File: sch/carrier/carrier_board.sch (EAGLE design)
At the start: 88 parts, among them CON1 SM03B-GHS-TB, CON2 SM03B-GHS-TB, Q1 SI7145, Q2 SI7145, Q3 SI7145, Q4 SIJ438DP, Q5 SIJ438DP, Q6 SIJ438DP, Q7 SIJ438DP, U1 LTV-355T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

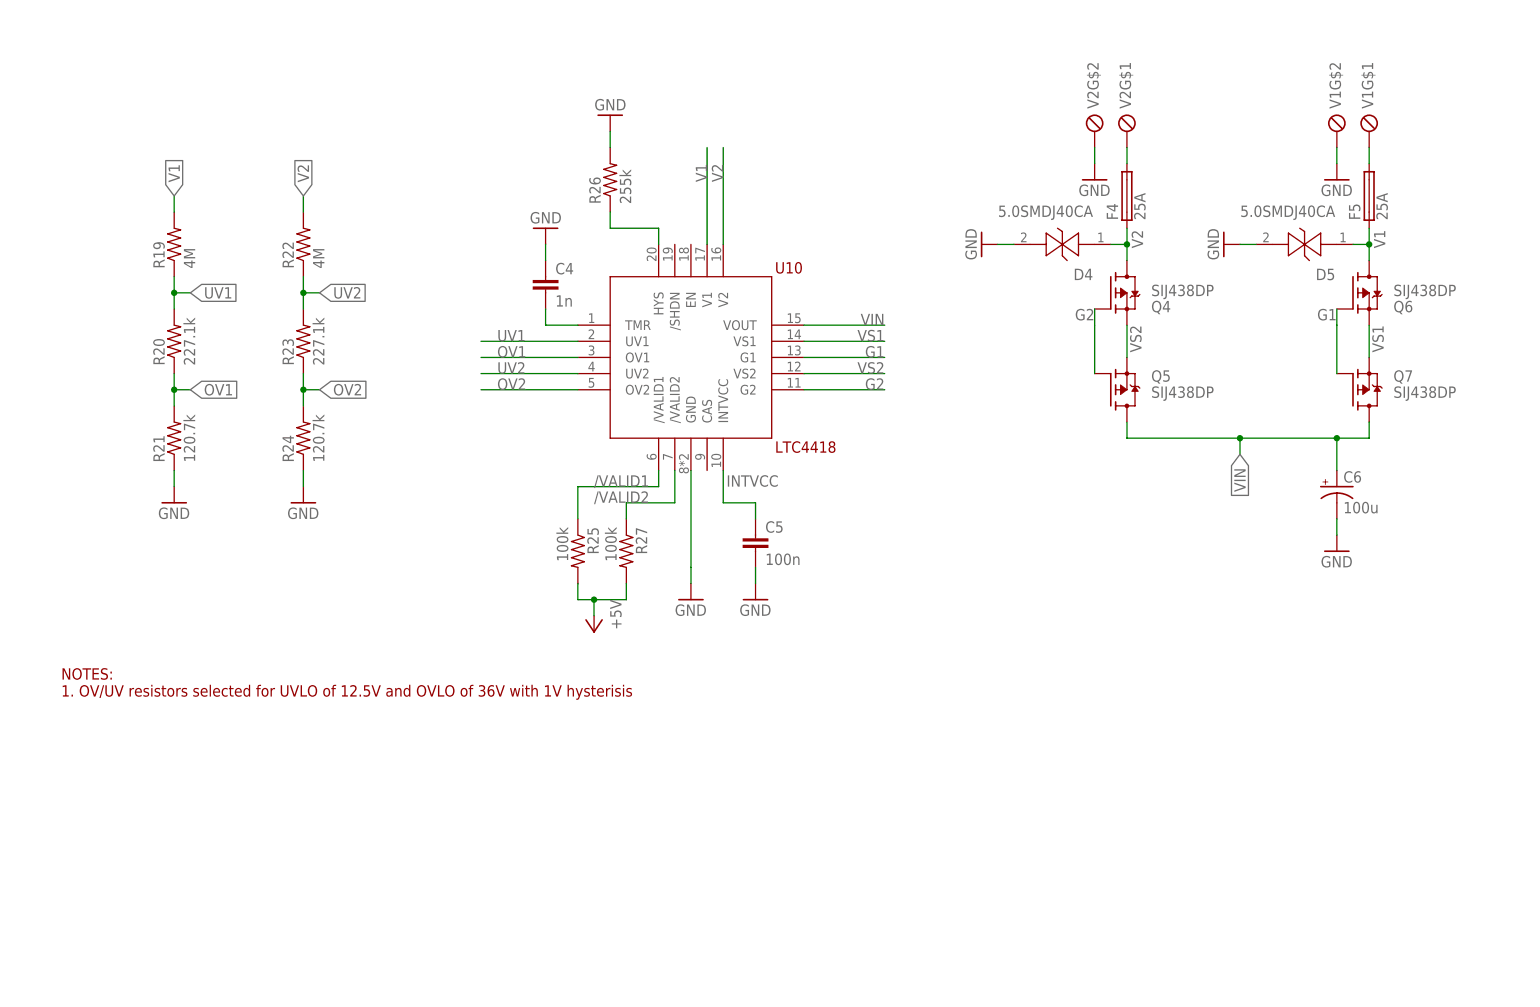
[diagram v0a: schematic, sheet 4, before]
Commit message: Added carrier BOM; Chaned carrier MOSFETs
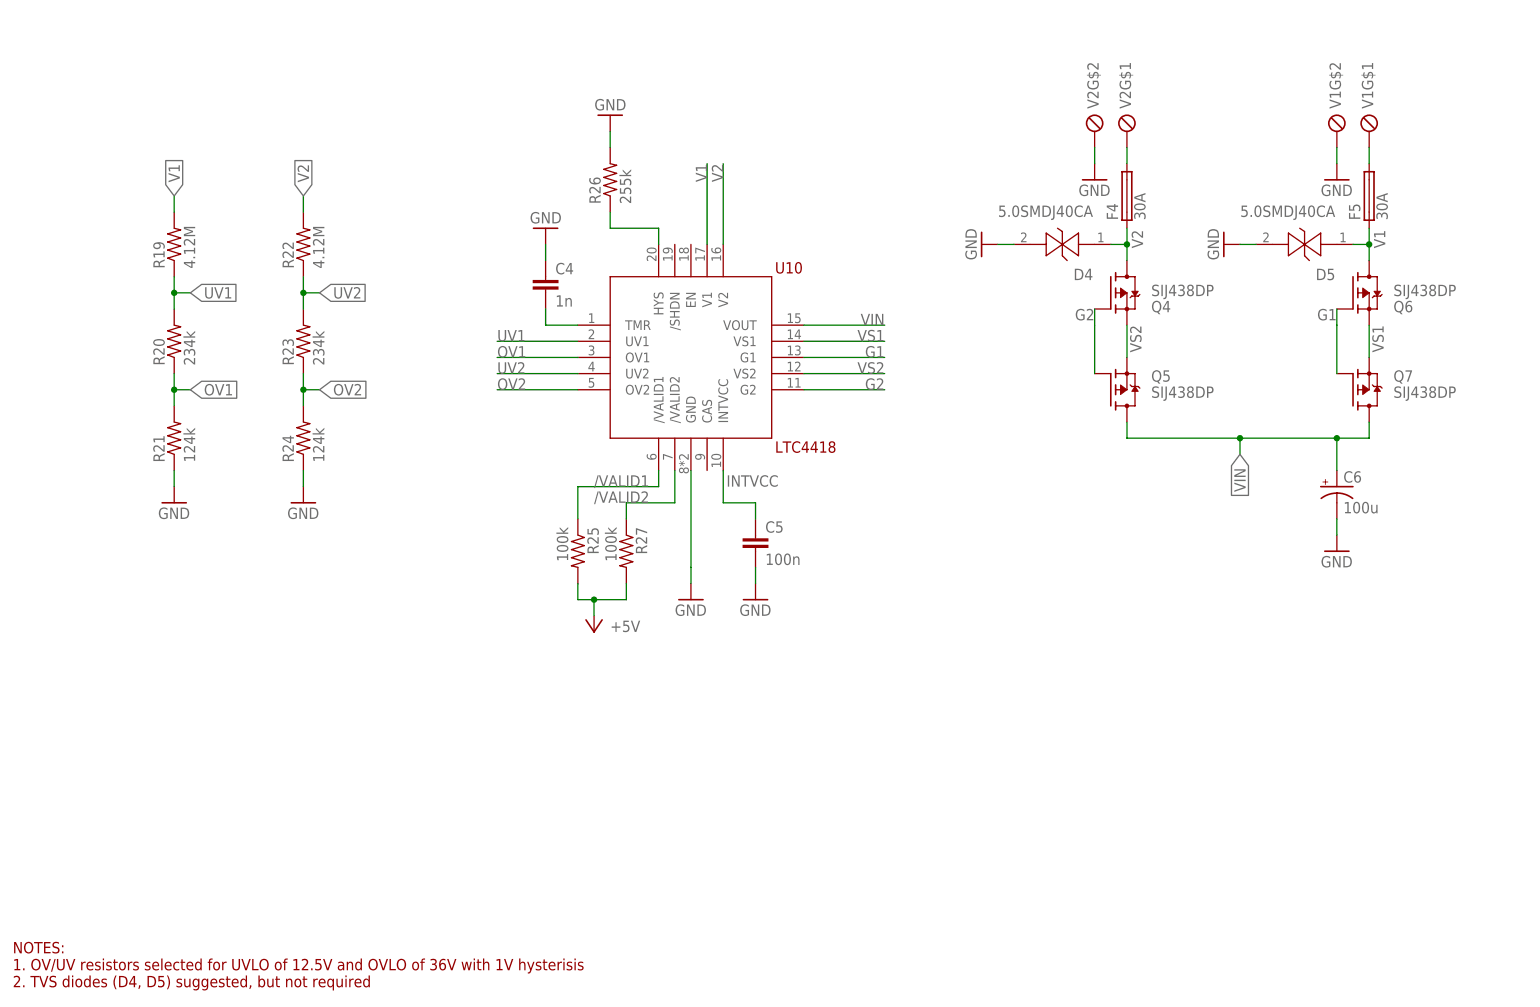
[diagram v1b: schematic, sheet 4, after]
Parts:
- F4, F5: value 25A -> 30A
- Q1, Q2, Q3: device LTM4607:SI7145 -> LTM4607:SIJ438DPPOWERPAK_SO8L
- Q4, Q5, Q6, Q7: device LTM4607:SIJ438DP -> LTM4607:SIJ438DPPOWERPAK_SO8L
- R19, R22: value 4M -> 4.12M
- R20, R23: value 227.1k -> 234k
- R21, R24: value 120.7k -> 124k
- R28, R29: device rcl:R-US_R1206 -> rcl:R-US_R0805
- R30, R33: value (none) -> 2k
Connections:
- net MCU_RUN1 renamed /MCU_RUN1
- net MCU_RUN2 renamed /MCU_RUN2
- net MCU_RUN3 renamed /MCU_RUN3
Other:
- note added: "NOTES: 1. OV/UV resistors selected for UVLO of 12.5V and OVLO of 36V with 1V hysterisis 2. TVS diodes (D4, D5) suggested, but not required"
- note added: "NOTES: 1. Short JP3 to turn on VOUT_SWITCHED nodes 2. Set /MCU_RUN pins to LOW to turn on converters. 3. Converters are on when no Teensy is present or if +5V supply (U13) fails. 4. LED1 and LED2 turn on when supply voltages are withn OV/UV window."
- note removed: "NOTES: 1. OV/UV resistors selected for UVLO of 12.5V and OVLO of 36V with 1V hysterisis"
- note removed: "NOTES: 1. Short JP3 to turn on VOUT_SWITCHED nodes"

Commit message: Revision 1.2
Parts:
- added C10, C9: 100n, rcl:C-EUC0603
- added Q8: BSS123, transistor-small-signal:BSS123
- added R35, R36: 1k, rcl:R-US_R0603
- C7, C8: value 10u -> 100n
- D4, D5: value 5.0SMDJ40CA -> SMBJ30CA; device 5.0SMDJ40CA:5.0SMDJ40CA -> LTM4607:SMBJ30CA
- Q1, Q2, Q3: value SI7145 -> SQJ407EP; device LTM4607:SIJ438DPPOWERPAK_SO8L -> LTM4607:SQJ407EP
- Q4, Q5, Q6, Q7: value SIJ438DP -> SI7145DP; device LTM4607:SIJ438DPPOWERPAK_SO8L -> LTM4607:SI7145
- R20, R23: value 234k -> 210k
- R21, R24: value 124k -> 150k
- R25, R27: device rcl:R-US_R0402 -> rcl:R-US_R0603
- U13: value (none) -> VX7805-500; device LTM4607:SRH05S05 -> LTM4607:0.1"_LINEAR_REGULATOR_REPLACEMENT
- X1, X3, X5: device LTM4607:282834-8 -> LTM4607:284391-6
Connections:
- new net G1_DRIVER: R36.1, U10.G1
- new net G2_DRIVER: R35.1, U10.G2
- new net N$10: Q8.G, U11.2
- net +5V: now also R25.1, R27.1; no longer R25.2, R27.2
- net /VALID1: now also R25.2, U11.14/A0; no longer R25.1, U11.13/SCK/LED
- net /VALID2: now also R27.2, U11.15/A1/T; no longer R27.1, U11.14/A0
- net G1: now also C10.2, R36.2; no longer U10.G1
- net G2: now also C9.2, R35.2; no longer U10.G2
- net GND: now also Q8.S, X1G$1.1, X1G$2.1, X1G$3.1, X3G$1.1, X3G$2.1, X3G$3.1, X5G$1.1, X5G$2.1, X5G$3.1; no longer X1$5.1, X1$6.1, X1$7.1, X1$8.1, X3$5.1, X3$6.1, X3$7.1, X3$8.1, X5$5.1, X5$6.1, X5$7.1, X5$8.1
- net INTVCC: now also U10./SHDN, U10.EN
- net KILL_SWITCH_C: now also Q8.D
- net VIN: now also C10.1, C9.1
- net VOUT1: now also X1G$5.1, X1G$6.1; no longer X1$1.1, X1$2.1
- net VOUT2: now also X3G$5.1, X3G$6.1; no longer X3$1.1, X3$2.1
- net VOUT3: now also X5G$5.1, X5G$6.1; no longer X5$1.1, X5$2.1
- net VOUT_SWITCHED1: now also X1G$4.1; no longer X1$3.1, X1$4.1
- net VOUT_SWITCHED2: now also X3G$4.1; no longer X3$3.1, X3$4.1
- net VOUT_SWITCHED3: now also X5G$4.1; no longer X5$3.1, X5$4.1
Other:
- note added: "NOTES: 1. OV/UV resistors selected for UVLO of 12.5V and OVLO of 30V with 1V hysterisis"
- note added: "NOTES: 1. Short JP3 to turn on VOUT_SWITCHED nodes 2. Set /MCU_RUN pins to LOW to turn on converters. 3. Converters remain on when no Teensy or +5V supply (U13) is present. 4. LED1 and LED2 turn on when supply voltages are within OV/UV window."
- note removed: "NOTES: 1. OV/UV resistors selected for UVLO of 12.5V and OVLO of 36V with 1V hysterisis 2. TVS diodes (D4, D5) suggested, but not required"
- note removed: "NOTES: 1. Short JP3 to turn on VOUT_SWITCHED nodes 2. Set /MCU_RUN pins to LOW to turn on converters. 3. Converters are on when no Teensy is present or if +5V supply (U13) fails. 4. LED1 and LED2 turn on when supply voltages are withn OV/UV window."
- moved on the sheet: C4, C5, C6, C7, C8, CON1-1, CON1-2, CON1-3, CON1-TABS, CON2-1, CON2-2, CON2-3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

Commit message: Carrier rev. 1.3
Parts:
- added D6, D7: (no value), LTM4607:SD0603S040S0R2
- added R37: 0, rcl:R-US_R0402
- R35, R36: value 1k -> 2k
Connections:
- net G1: now also D7.C
- net G1_DRIVER: now also D7.A
- net G2: now also D6.C
- net G2_DRIVER: now also D6.A
- net INTVCC: now also R37.1
- net TMR: now also R37.2
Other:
- note added: "NOTES: 1. OV/UV resistors selected for UVLO of 12.5V and OVLO of 30V with 1V hysterisis 2. Populate R37 to enable shortest voltage source validation time 3. Low impedance input source recommended to prevent motor-boating effect"
- note removed: "NOTES: 1. OV/UV resistors selected for UVLO of 12.5V and OVLO of 30V with 1V hysterisis"
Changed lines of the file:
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@@
 <part name="C9" library="rcl" library_urn="urn:adsk.eagle:library:334" deviceset="C-EU" device="C0603" package3d_urn="urn:adsk.eagle:package:23616/2" value="100n"/>
 <part name="C10" library="rcl" library_urn="urn:adsk.eagle:library:334" deviceset="C-EU" device="C0603" package3d_urn="urn:adsk.eagle:package:23616/2" value="100n"/>
-<part name="R35" library="rcl" library_urn="urn:adsk.eagle:library:334" deviceset="R-US_" device="R0603" package3d_urn="urn:adsk.eagle:package:23555/2" value="1k"/>
-<part name="R36" library="rcl" library_urn="urn:adsk.eagle:library:334" deviceset="R-US_" device="R0603" package3d_urn="urn:adsk.eagle:package:23555/2" value="1k"/>
+<part name="R35" library="rcl" library_urn="urn:adsk.eagle:library:334" deviceset="R-US_" device="R0603" package3d_urn="urn:adsk.eagle:package:23555/2" value="2k"/>
+<part name="R36" library="rcl" library_urn="urn:adsk.eagle:library:334" deviceset="R-US_" device="R0603" package3d_urn="urn:adsk.eagle:package:23555/2" value="2k"/>
+<part name="D6" library="LTM4607" deviceset="SD0603S040S0R2" device=""/>
+<part name="D7" library="LTM4607" deviceset="SD0603S040S0R2" device=""/>
+<part name="R37" library="rcl" library_urn="urn:adsk.eagle:library:334" deviceset="R-US_" device="R0402" package3d_urn="urn:adsk.eagle:package:23547/2" value="0"/>
 </parts>
 <sheets>
@@
 <plain>
 <text x="12.7" y="10.16" size="1.778" layer="94">NOTES:
-1. OV/UV resistors selected for UVLO of 12.5V and OVLO of 30V with 1V hysterisis</text>
+1. OV/UV resistors selected for UVLO of 12.5V and OVLO of 30V with 1V hysterisis
+2. Populate R37 to enable shortest voltage source validation time
+3. Low impedance input source recommended to prevent motor-boating effect</text>
 </plain>
 <instances>
@@
 <attribute name="NAME" x="212.09" y="115.7986" size="1.778" layer="95"/>
 <attribute name="VALUE" x="212.09" y="110.998" size="1.778" layer="96"/>
+</instance>
+<instance part="D6" gate="G$1" x="165.1" y="121.92" smashed="yes">
+<attribute name="NAME" x="162.814" y="123.825" size="1.778" layer="95"/>
+<attribute name="VALUE" x="162.814" y="118.491" size="1.778" layer="96"/>
+</instance>
+<instance part="D7" gate="G$1" x="215.9" y="121.92" smashed="yes">
+<attribute name="NAME" x="213.614" y="123.825" size="1.778" layer="95"/>
+<attribute name="VALUE" x="213.614" y="118.491" size="1.778" layer="96"/>
+</instance>
+<instance part="R37" gate="G$1" x="71.12" y="134.62" smashed="yes" rot="R270">
+<attribute name="NAME" x="72.6186" y="138.43" size="1.778" layer="95" rot="R270"/>
+<attribute name="VALUE" x="67.818" y="138.43" size="1.778" layer="96" rot="R270"/>
 </instance>
 </instances>
@@
 <wire x1="170.18" y1="114.3" x2="172.72" y2="114.3" width="0.1524" layer="91"/>
 <junction x="172.72" y="114.3"/>
+<pinref part="D6" gate="G$1" pin="C"/>
+<wire x1="167.64" y1="121.92" x2="170.18" y2="121.92" width="0.1524" layer="91"/>
+<wire x1="170.18" y1="121.92" x2="170.18" y2="114.3" width="0.1524" layer="91"/>
+<junction x="170.18" y="114.3"/>
 </segment>
 </net>
@@
 <wire x1="220.98" y1="114.3" x2="223.52" y2="114.3" width="0.1524" layer="91"/>
 <junction x="223.52" y="114.3"/>
+<pinref part="D7" gate="G$1" pin="C"/>
+<wire x1="218.44" y1="121.92" x2="220.98" y2="121.92" width="0.1524" layer="91"/>
+<wire x1="220.98" y1="121.92" x2="220.98" y2="114.3" width="0.1524" layer="91"/>
+<junction x="220.98" y="114.3"/>
 </segment>
 </net>
@@
 <pinref part="C4" gate="G$1" pin="2"/>
 <wire x1="78.74" y1="129.54" x2="78.74" y2="127" width="0.1524" layer="91"/>
+<pinref part="R37" gate="G$1" pin="2"/>
+<wire x1="71.12" y1="129.54" x2="71.12" y2="127" width="0.1524" layer="91"/>
+<wire x1="71.12" y1="127" x2="78.74" y2="127" width="0.1524" layer="91"/>
+<junction x="78.74" y="127"/>
 </segment>
 </net>
@@
 <wire x1="101.6" y1="139.7" x2="101.6" y2="152.4" width="0.1524" layer="91"/>
 <label x="101.6" y="152.4" size="1.778" layer="95" rot="R90" align="bottom-right"/>
+</segment>
+<segment>
+<pinref part="R37" gate="G$1" pin="1"/>
+<wire x1="71.12" y1="139.7" x2="71.12" y2="152.4" width="0.1524" layer="91"/>
+<label x="71.12" y="152.4" size="1.778" layer="95" rot="MR270"/>
 </segment>
 </net>
@@
 <wire x1="160.02" y1="114.3" x2="144.78" y2="114.3" width="0.1524" layer="91"/>
 <label x="144.78" y="114.3" size="1.778" layer="95"/>
+<pinref part="D6" gate="G$1" pin="A"/>
+<wire x1="162.56" y1="121.92" x2="160.02" y2="121.92" width="0.1524" layer="91"/>
+<wire x1="160.02" y1="121.92" x2="160.02" y2="114.3" width="0.1524" layer="91"/>
+<junction x="160.02" y="114.3"/>
 </segment>
 </net>
@@
 <wire x1="210.82" y1="114.3" x2="195.58" y2="114.3" width="0.1524" layer="91"/>
 <label x="195.58" y="114.3" size="1.778" layer="95"/>
-</segment>
-</net>
+<pinref part="D7" gate="G$1" pin="A"/>
+<wire x1="213.36" y1="121.92" x2="210.82" y2="121.92" width="0.1524" layer="91"/>
+<wire x1="210.82" y1="121.92" x2="210.82" y2="114.3" width="0.1524" layer="91"/>
+<junction x="210.82" y="114.3"/>
+</segment>
+</net>

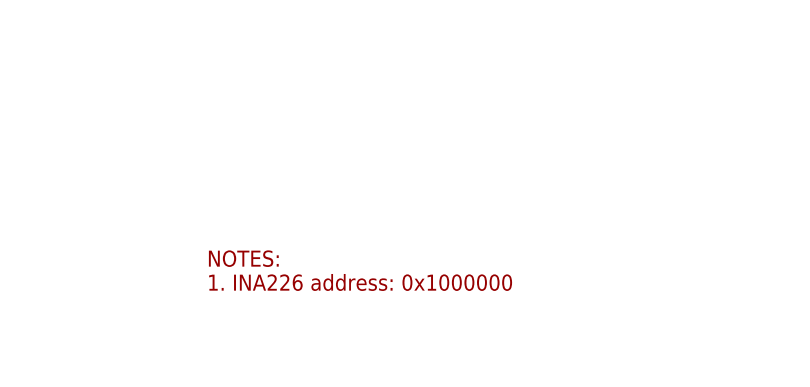
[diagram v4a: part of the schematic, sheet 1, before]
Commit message: Fixed typo in sch
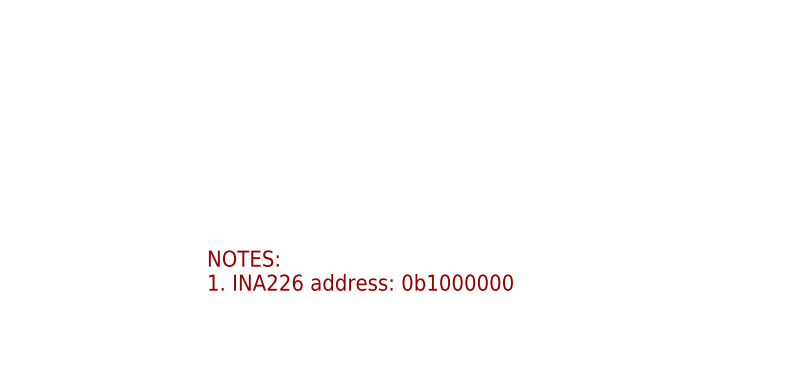
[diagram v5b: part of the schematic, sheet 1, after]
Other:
- note added: "NOTES: 1. INA226 address: 0b1000000"
- note added: "NOTES: 1. INA226 address: 0b1000001"
- note added: "NOTES: 1. INA226 address: 0b1000010"
- note removed: "NOTES: 1. INA226 address: 0x1000000"
- note removed: "NOTES: 1. INA226 address: 0x1000001"
- note removed: "NOTES: 1. INA226 address: 0x1000010"
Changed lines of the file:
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@@
 <plain>
 <text x="162.56" y="27.94" size="1.778" layer="94">NOTES:
-1. INA226 address: 0x1000000</text>
+1. INA226 address: 0b1000000</text>
 </plain>
 <instances>
@@
 <plain>
 <text x="162.56" y="27.94" size="1.778" layer="94">NOTES:
-1. INA226 address: 0x1000001</text>
+1. INA226 address: 0b1000001</text>
 </plain>
 <instances>
@@
 <plain>
 <text x="162.56" y="27.94" size="1.778" layer="94">NOTES:
-1. INA226 address: 0x1000010</text>
+1. INA226 address: 0b1000010</text>
 </plain>
 <instances>

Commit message: Carrier rev. 1.4
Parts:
- added D8: MBRS2040LT3G, diode:MBRS130LT3
- added R38: 50k, rcl:R-US_R0603
- added R39: 5k, rcl:R-US_R0603
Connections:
- new net N$11: D8.C, U13.VIN
- new net V1_ANALOG_IN: R38.1, R39.2, U11.17/A3/T
- net GND: now also R39.1
- net N$1: now also D8.A, R38.2; no longer U13.VIN
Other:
- moved on the sheet: F6, U13
